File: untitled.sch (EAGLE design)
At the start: 24 parts

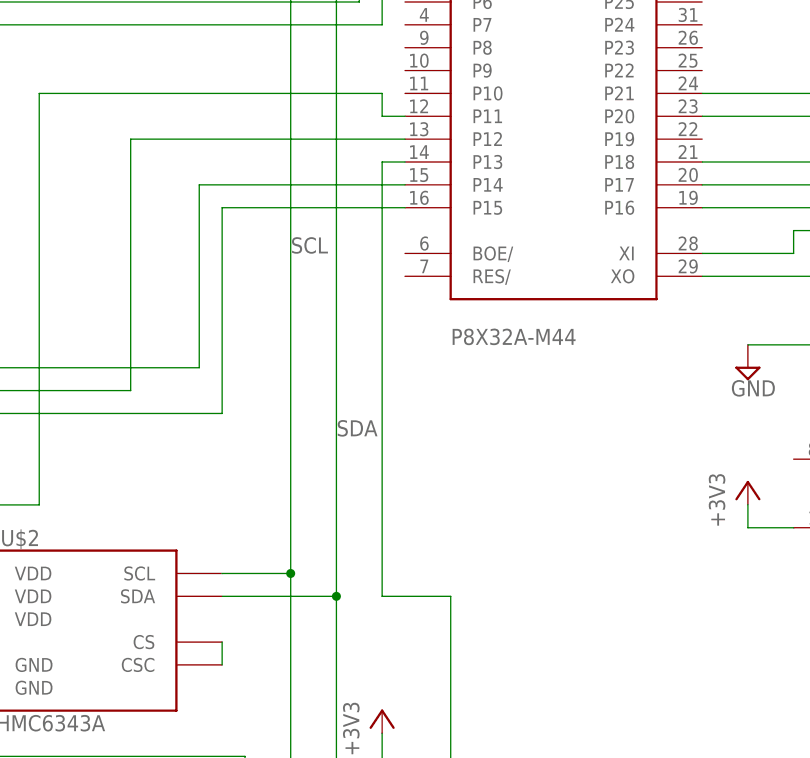
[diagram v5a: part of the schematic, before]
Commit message: Connected BOEn to GND
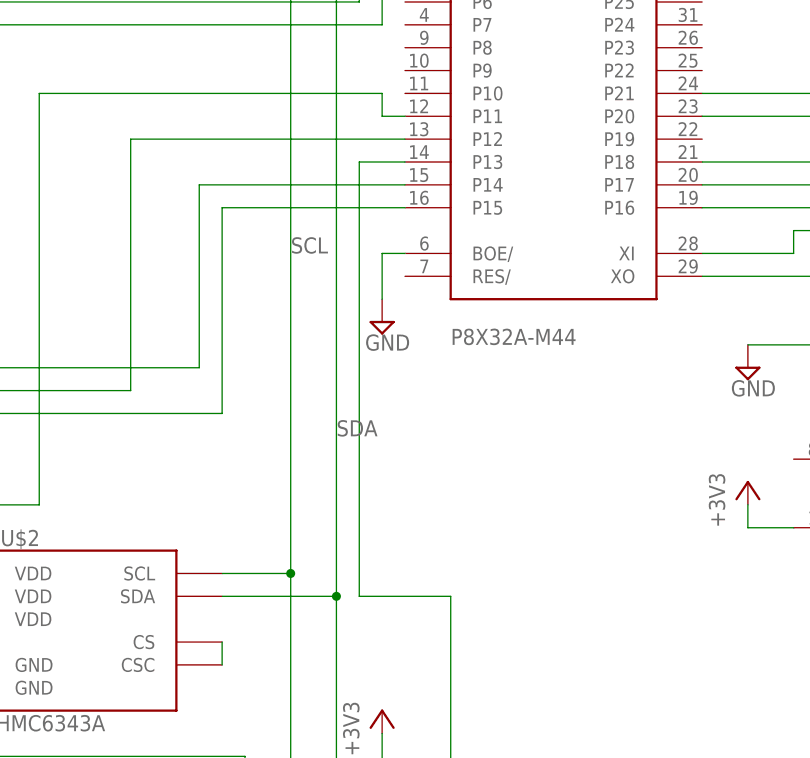
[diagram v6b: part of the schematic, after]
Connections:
- net GND: now also U$1G$1.BOE/
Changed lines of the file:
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@@
 <part name="C2" library="rcl" deviceset="C-US" device="C0603"/>
 <part name="C3" library="rcl" deviceset="C-US" device="C0603"/>
+<part name="SUPPLY8" library="supply2" deviceset="GND" device=""/>
 </parts>
 <sheets>
@@
 <instance part="C2" gate="G$1" x="-2.54" y="109.22"/>
 <instance part="C3" gate="G$1" x="5.08" y="104.14"/>
+<instance part="SUPPLY8" gate="GND" x="7.62" y="33.02"/>
 </instances>
 <busses>
@@
 <segment>
 <pinref part="U$1" gate="G$1" pin="P13"/>
-<wire x1="10.16" y1="50.8" x2="7.62" y2="50.8" width="0.1524" layer="91"/>
-<wire x1="7.62" y1="50.8" x2="7.62" y2="2.54" width="0.1524" layer="91"/>
-<wire x1="7.62" y1="2.54" x2="15.24" y2="2.54" width="0.1524" layer="91"/>
+<wire x1="10.16" y1="50.8" x2="5.08" y2="50.8" width="0.1524" layer="91"/>
+<wire x1="5.08" y1="50.8" x2="5.08" y2="2.54" width="0.1524" layer="91"/>
+<wire x1="5.08" y1="2.54" x2="15.24" y2="2.54" width="0.1524" layer="91"/>
 <wire x1="15.24" y1="2.54" x2="15.24" y2="-45.72" width="0.1524" layer="91"/>
 <wire x1="15.24" y1="-45.72" x2="-83.82" y2="-45.72" width="0.1524" layer="91"/>
@@
 <junction x="33.02" y="96.52"/>
 </segment>
-</net>
+<segment>
+<pinref part="U$1" gate="G$1" pin="BOE/"/>
+<pinref part="SUPPLY8" gate="GND" pin="GND"/>
+<wire x1="10.16" y1="40.64" x2="7.62" y2="40.64" width="0.1524" layer="91"/>
+<wire x1="7.62" y1="40.64" x2="7.62" y2="35.56" width="0.1524" layer="91"/>
+</segment>
+</net>

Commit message: Finished PCB V2
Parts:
- added C4: (no value), SparkFun:CAP0603
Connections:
- net +3V3: now also C4.1, GPS.VBACKUP, GPS.VCC
- net GND: now also C4.2, GPS.GND@1
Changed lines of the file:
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@@
 <part name="C3" library="rcl" deviceset="C-US" device="C0603"/>
 <part name="SUPPLY8" library="supply2" deviceset="GND" device=""/>
+<part name="C4" library="SparkFun" deviceset="CAP" device="0603"/>
+<part name="SUPPLY9" library="supply2" deviceset="GND" device=""/>
+<part name="+3V9" library="supply1" deviceset="+3V3" device=""/>
 </parts>
 <sheets>
@@
 <instance part="C3" gate="G$1" x="5.08" y="104.14"/>
 <instance part="SUPPLY8" gate="GND" x="7.62" y="33.02"/>
+<instance part="C4" gate="G$1" x="-7.62" y="15.24"/>
+<instance part="SUPPLY9" gate="GND" x="-7.62" y="7.62"/>
+<instance part="+3V9" gate="G$1" x="-7.62" y="25.4"/>
 </instances>
 <busses>
@@
 <junction x="165.1" y="48.26"/>
 <pinref part="GPS" gate="G$1" pin="GND@2"/>
-<wire x1="160.02" y1="66.04" x2="154.94" y2="66.04" width="0.1524" layer="91"/>
+<wire x1="160.02" y1="66.04" x2="157.48" y2="66.04" width="0.1524" layer="91"/>
+<wire x1="157.48" y1="66.04" x2="154.94" y2="66.04" width="0.1524" layer="91"/>
 <wire x1="154.94" y1="66.04" x2="154.94" y2="48.26" width="0.1524" layer="91"/>
 <wire x1="160.02" y1="48.26" x2="154.94" y2="48.26" width="0.1524" layer="91"/>
 <junction x="160.02" y="48.26"/>
+<pinref part="GPS" gate="G$1" pin="GND@1"/>
+<wire x1="160.02" y1="78.74" x2="157.48" y2="78.74" width="0.1524" layer="91"/>
+<wire x1="157.48" y1="78.74" x2="157.48" y2="66.04" width="0.1524" layer="91"/>
+<junction x="157.48" y="66.04"/>
 </segment>
 <segment>
@@
 <wire x1="7.62" y1="40.64" x2="7.62" y2="35.56" width="0.1524" layer="91"/>
 </segment>
+<segment>
+<pinref part="C4" gate="G$1" pin="2"/>
+<pinref part="SUPPLY9" gate="GND" pin="GND"/>
+<wire x1="-7.62" y1="12.7" x2="-7.62" y2="10.16" width="0.1524" layer="91"/>
+</segment>
 </net>
 <net name="+5V" class="0">
@@
 <pinref part="+3V7" gate="G$1" pin="+3V3"/>
 <wire x1="154.94" y1="86.36" x2="154.94" y2="83.82" width="0.1524" layer="91"/>
-<wire x1="162.56" y1="83.82" x2="154.94" y2="83.82" width="0.1524" layer="91"/>
-<junction x="154.94" y="83.82"/>
-<wire x1="154.94" y1="83.82" x2="154.94" y2="68.58" width="0.1524" layer="91"/>
+<wire x1="154.94" y1="83.82" x2="154.94" y2="76.2" width="0.1524" layer="91"/>
+<wire x1="154.94" y1="76.2" x2="154.94" y2="68.58" width="0.1524" layer="91"/>
 <wire x1="154.94" y1="68.58" x2="152.4" y2="68.58" width="0.1524" layer="91"/>
 <wire x1="152.4" y1="68.58" x2="152.4" y2="50.8" width="0.1524" layer="91"/>
@@
 <wire x1="132.08" y1="50.8" x2="132.08" y2="25.4" width="0.1524" layer="91"/>
 <pinref part="10EEPROM" gate="G$1" pin="1"/>
+<pinref part="GPS" gate="G$1" pin="VCC"/>
+<wire x1="160.02" y1="83.82" x2="154.94" y2="83.82" width="0.1524" layer="91"/>
+<junction x="154.94" y="83.82"/>
+<pinref part="GPS" gate="G$1" pin="VBACKUP"/>
+<wire x1="160.02" y1="76.2" x2="154.94" y2="76.2" width="0.1524" layer="91"/>
+<junction x="154.94" y="76.2"/>
 </segment>
 <segment>
@@
 <junction x="10.16" y="109.22"/>
 </segment>
-</net>
+<segment>
+<pinref part="+3V9" gate="G$1" pin="+3V3"/>
+<pinref part="C4" gate="G$1" pin="1"/>
+<wire x1="-7.62" y1="22.86" x2="-7.62" y2="20.32" width="0.1524" layer="91"/>
+</segment>
+</net>

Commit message: more clean up, with work based off amatus's designs
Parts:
- 3.3LDO: value LDO1117-33 -> REG1117X; device ldo1117-33:LDO1117-33 -> burr-brown:REG1117X
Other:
- moved on the sheet: 3.3LDO
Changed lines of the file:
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@@
 <part name="OLED_SCREEN" library="4dScreen" deviceset="4DSCREEN" device=""/>
 <part name="LIPOCHARGER-BOOSTER" library="SFLipoPack" deviceset="SFLIPO" device=""/>
-<part name="3.3LDO" library="ldo1117-33" deviceset="LDO1117-33" device=""/>
 <part name="5WAYSWITCH" library="5-wayswitch" deviceset="5-WAYSWITCH" device=""/>
 <part name="EEPROM" library="adafruit" deviceset="DS1307" device=""/>
@@
 <part name="SUPPLY9" library="supply2" deviceset="GND" device=""/>
 <part name="+3V9" library="supply1" deviceset="+3V3" device=""/>
+<part name="3.3LDO" library="burr-brown" deviceset="REG1117" device="X"/>
 </parts>
 <sheets>
@@
 <instance part="OLED_SCREEN" gate="G$1" x="-68.58" y="68.58"/>
 <instance part="LIPOCHARGER-BOOSTER" gate="G$1" x="-111.76" y="96.52"/>
-<instance part="3.3LDO" gate="G$1" x="-66.04" y="88.9" rot="R270"/>
 <instance part="5WAYSWITCH" gate="G$1" x="-71.12" y="0"/>
 <instance part="EEPROM" gate="G$1" x="165.1" y="27.94"/>
@@
 <instance part="SUPPLY6" gate="GND" x="165.1" y="10.16"/>
 <instance part="P+2" gate="1" x="-83.82" y="104.14"/>
-<instance part="+3V1" gate="G$1" x="-76.2" y="104.14"/>
+<instance part="+3V1" gate="G$1" x="-40.64" y="106.68"/>
 <instance part="+3V2" gate="G$1" x="-109.22" y="33.02"/>
 <instance part="+3V3" gate="G$1" x="-25.4" y="96.52"/>
@@
 <instance part="SUPPLY9" gate="GND" x="-7.62" y="7.62"/>
 <instance part="+3V9" gate="G$1" x="-7.62" y="25.4"/>
+<instance part="3.3LDO" gate="G$1" x="-55.88" y="96.52"/>
 </instances>
 <busses>
@@
 <wire x1="-86.36" y1="76.2" x2="-86.36" y2="83.82" width="0.1524" layer="91"/>
 <junction x="-86.36" y="83.82"/>
-<pinref part="3.3LDO" gate="G$1" pin="GND"/>
 <wire x1="-86.36" y1="93.98" x2="-73.66" y2="93.98" width="0.1524" layer="91"/>
 <junction x="-86.36" y="93.98"/>
+<wire x1="-73.66" y1="93.98" x2="-73.66" y2="83.82" width="0.1524" layer="91"/>
+<pinref part="3.3LDO" gate="G$1" pin="GND"/>
+<wire x1="-73.66" y1="83.82" x2="-55.88" y2="83.82" width="0.1524" layer="91"/>
 </segment>
 <segment>
@@
 <pinref part="LIPOCHARGER-BOOSTER" gate="G$1" pin="P$2"/>
 <wire x1="-104.14" y1="99.06" x2="-83.82" y2="99.06" width="0.1524" layer="91"/>
-<wire x1="-83.82" y1="99.06" x2="-83.82" y2="83.82" width="0.1524" layer="91"/>
-<wire x1="-83.82" y1="83.82" x2="-73.66" y2="83.82" width="0.1524" layer="91"/>
-<pinref part="3.3LDO" gate="G$1" pin="VIN"/>
+<wire x1="-83.82" y1="99.06" x2="-83.82" y2="96.52" width="0.1524" layer="91"/>
+<wire x1="-83.82" y1="96.52" x2="-83.82" y2="76.2" width="0.1524" layer="91"/>
 <junction x="-83.82" y="99.06"/>
 <pinref part="P+2" gate="1" pin="+5V"/>
 <wire x1="-83.82" y1="101.6" x2="-83.82" y2="99.06" width="0.1524" layer="91"/>
-<wire x1="-83.82" y1="83.82" x2="-83.82" y2="76.2" width="0.1524" layer="91"/>
 <wire x1="-83.82" y1="76.2" x2="-58.42" y2="76.2" width="0.1524" layer="91"/>
-<junction x="-83.82" y="83.82"/>
 <pinref part="OLED_SCREEN" gate="G$1" pin="5V"/>
 <wire x1="-58.42" y1="76.2" x2="-58.42" y2="71.12" width="0.1524" layer="91"/>
 <wire x1="-58.42" y1="71.12" x2="-60.96" y2="71.12" width="0.1524" layer="91"/>
+<pinref part="3.3LDO" gate="G$1" pin="VIN"/>
+<wire x1="-83.82" y1="96.52" x2="-68.58" y2="96.52" width="0.1524" layer="91"/>
+<junction x="-83.82" y="96.52"/>
 </segment>
 </net>
 <net name="+3V3" class="0">
-<segment>
-<pinref part="+3V1" gate="G$1" pin="+3V3"/>
-<pinref part="3.3LDO" gate="G$1" pin="VOUT"/>
-<wire x1="-76.2" y1="101.6" x2="-76.2" y2="88.9" width="0.1524" layer="91"/>
-<wire x1="-76.2" y1="88.9" x2="-73.66" y2="88.9" width="0.1524" layer="91"/>
-</segment>
 <segment>
 <pinref part="I2C5" gate="G$1" pin="1"/>
@@
 <wire x1="-7.62" y1="22.86" x2="-7.62" y2="20.32" width="0.1524" layer="91"/>
 </segment>
-</net>
+<segment>
+<pinref part="3.3LDO" gate="G$1" pin="VOUT"/>
+<wire x1="-43.18" y1="96.52" x2="-40.64" y2="96.52" width="0.1524" layer="91"/>
+<pinref part="+3V1" gate="G$1" pin="+3V3"/>
+<wire x1="-40.64" y1="96.52" x2="-40.64" y2="104.14" width="0.1524" layer="91"/>
+</segment>
+</net>
